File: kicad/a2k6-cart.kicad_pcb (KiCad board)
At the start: 2 copper layers, 41.4 x 47.8 mm, 4 parts, among them J1 2600_Cartridge_Port, U1 2732, U2 74LS04

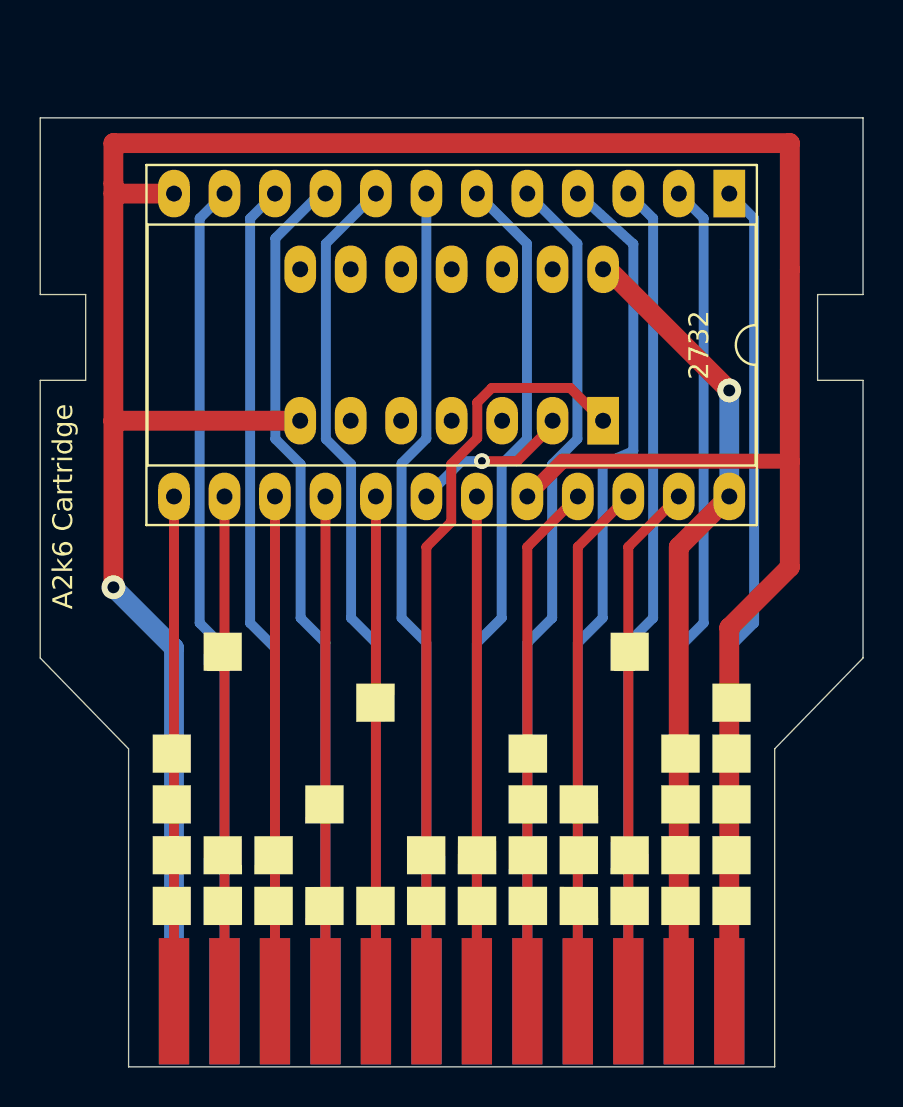
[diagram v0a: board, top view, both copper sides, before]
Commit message: Updated to use a ribbon cable connector.
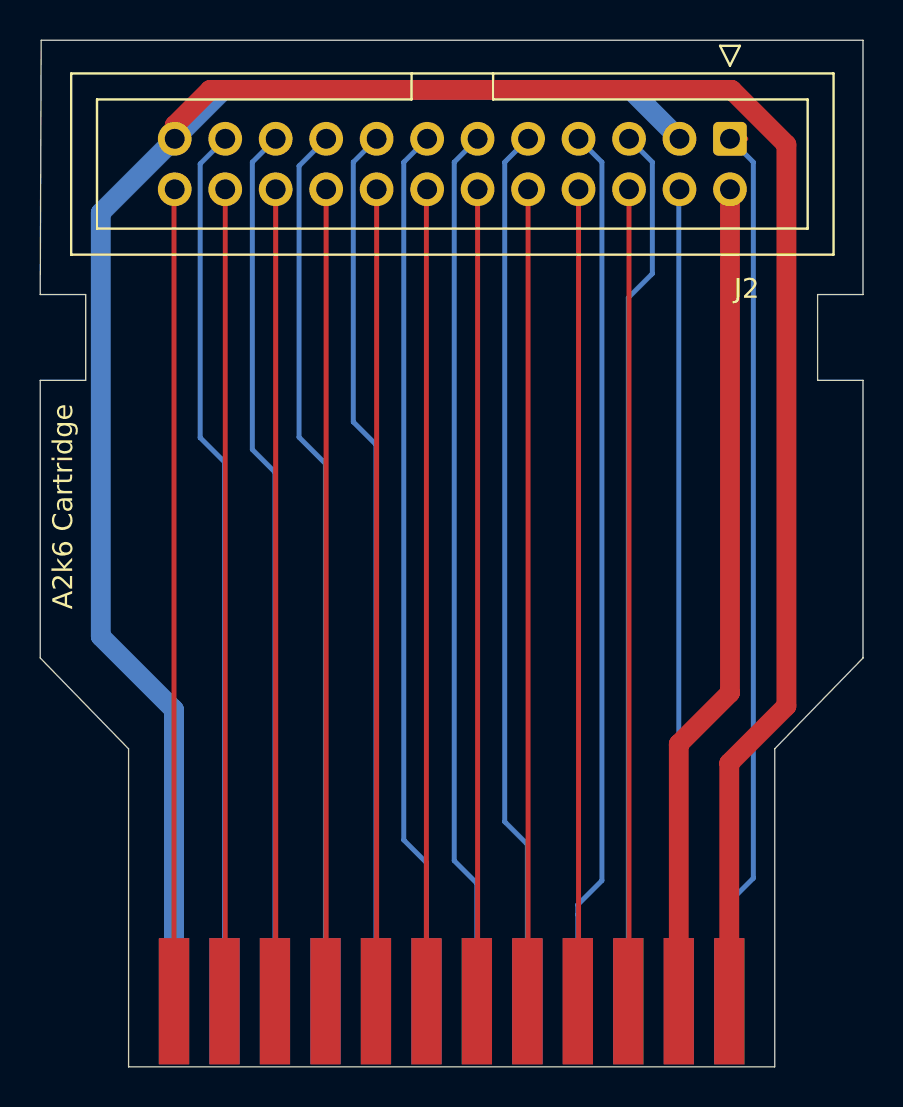
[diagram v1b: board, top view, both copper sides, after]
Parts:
- removed G***: LOGO, atari26k-cart:pattern
- removed U1: 2732, Package_DIP:DIP-24_W15.24mm_Socket_LongPads
- removed U2: 74LS04, Package_DIP:DIP-14_W7.62mm_LongPads
- added J2: Conn_02x12, Connector_IDC:IDC-Header_2x12_P2.54mm_Vertical, F.Cu at (166.7, 74.5)
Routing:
- net Net-(J2-Pin_12): track 25.4 -> 40.9 mm
- net D7: track 25.4 -> 40.9 mm
- net D6: track 25.4 -> 40.9 mm
- net D5: track 25.4 -> 40.9 mm
- net D4: track 25.4 -> 40.9 mm
- net D3: track 25.4 -> 40.9 mm
- net Net-(J2-Pin_6): track 26.5 -> 40.9 mm
- net Net-(J2-Pin_10): track 26.5 -> 40.9 mm
- net Net-(J2-Pin_8): track 26.5 -> 40.9 mm
- net Net-(U1-Pad18): track 8.45 -> 0.00 mm, vias 1 -> 0
- net Net-(J2-Pin_1): track 41.7 -> 45.2 mm
- net D2: track 41.7 -> 44.4 mm
- net Net-(J2-Pin_5): track 41.7 -> 44.4 mm
- net Net-(J2-Pin_13): track 41.7 -> 44.4 mm
- net D1: track 41.7 -> 44.4 mm
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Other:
- board size 41.4 x 47.8 mm -> 41.4 x 51.7 mm
- net class Default removed
